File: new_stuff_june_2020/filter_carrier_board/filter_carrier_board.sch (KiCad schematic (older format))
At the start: 44 parts, among them J1 CV_inputs, J10 Conn_02x05_Odd_Even, J2 signal_inputs, J3 dry_out, J4 Conn_01x04, J5 Conn_01x04, J6 CV_out, J7 Conn_01x04, J8 Conn_01x08, J9 wet_out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

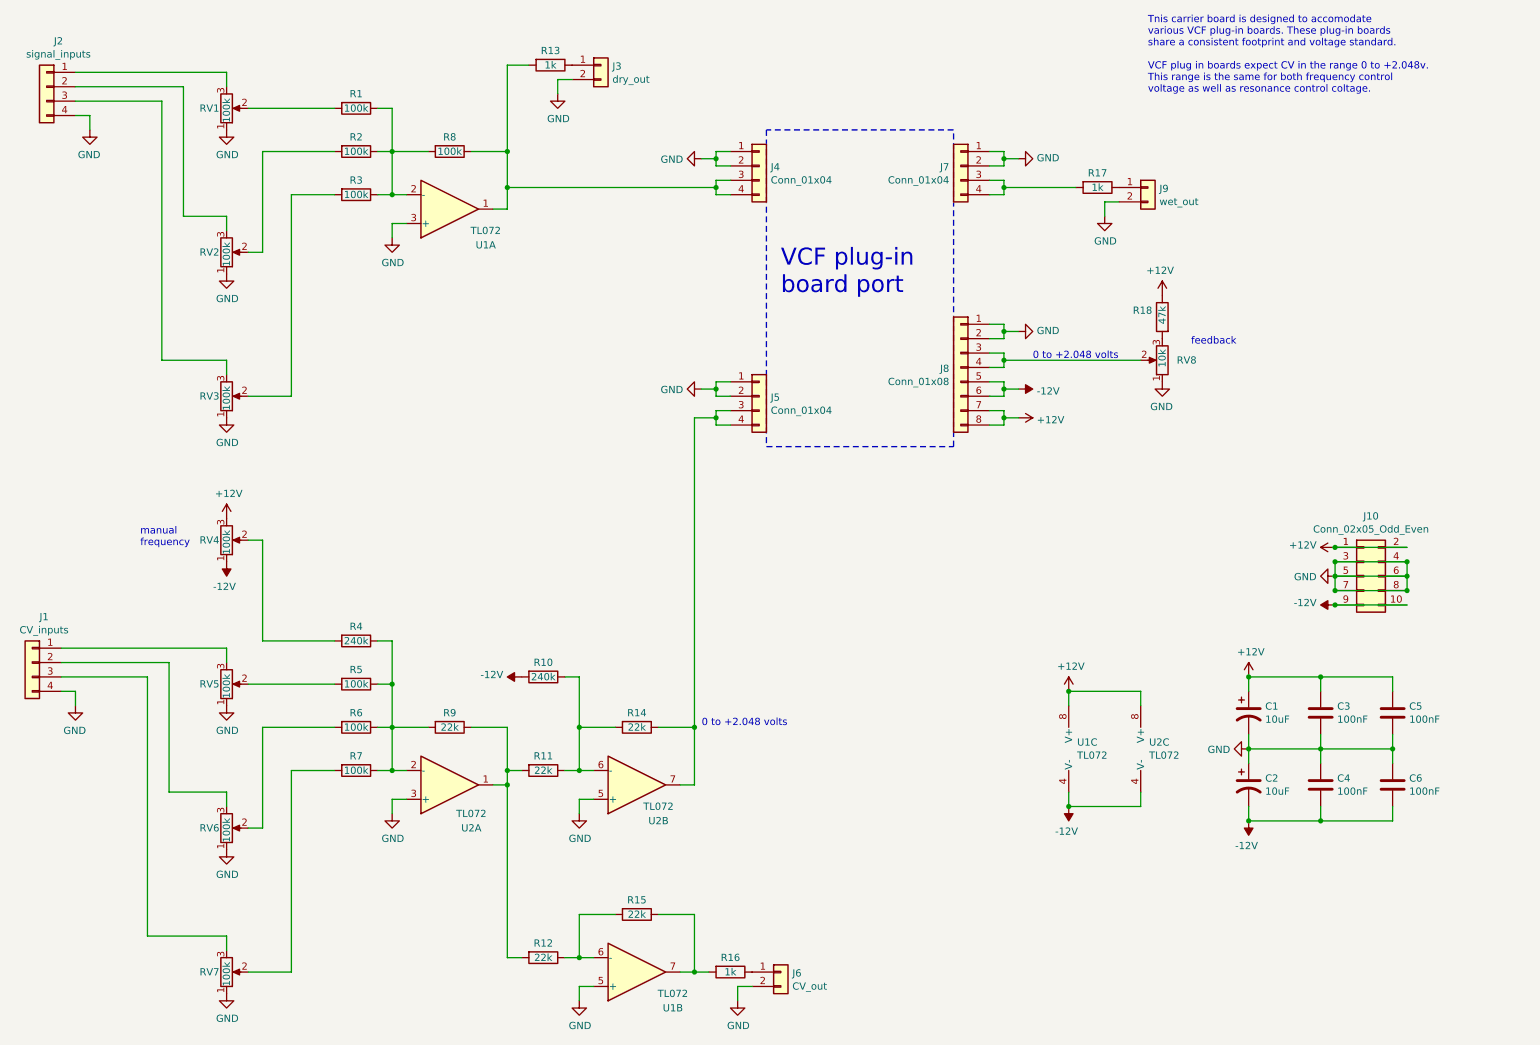
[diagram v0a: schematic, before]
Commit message: add +/- 5 volt ref to VCF carrier board
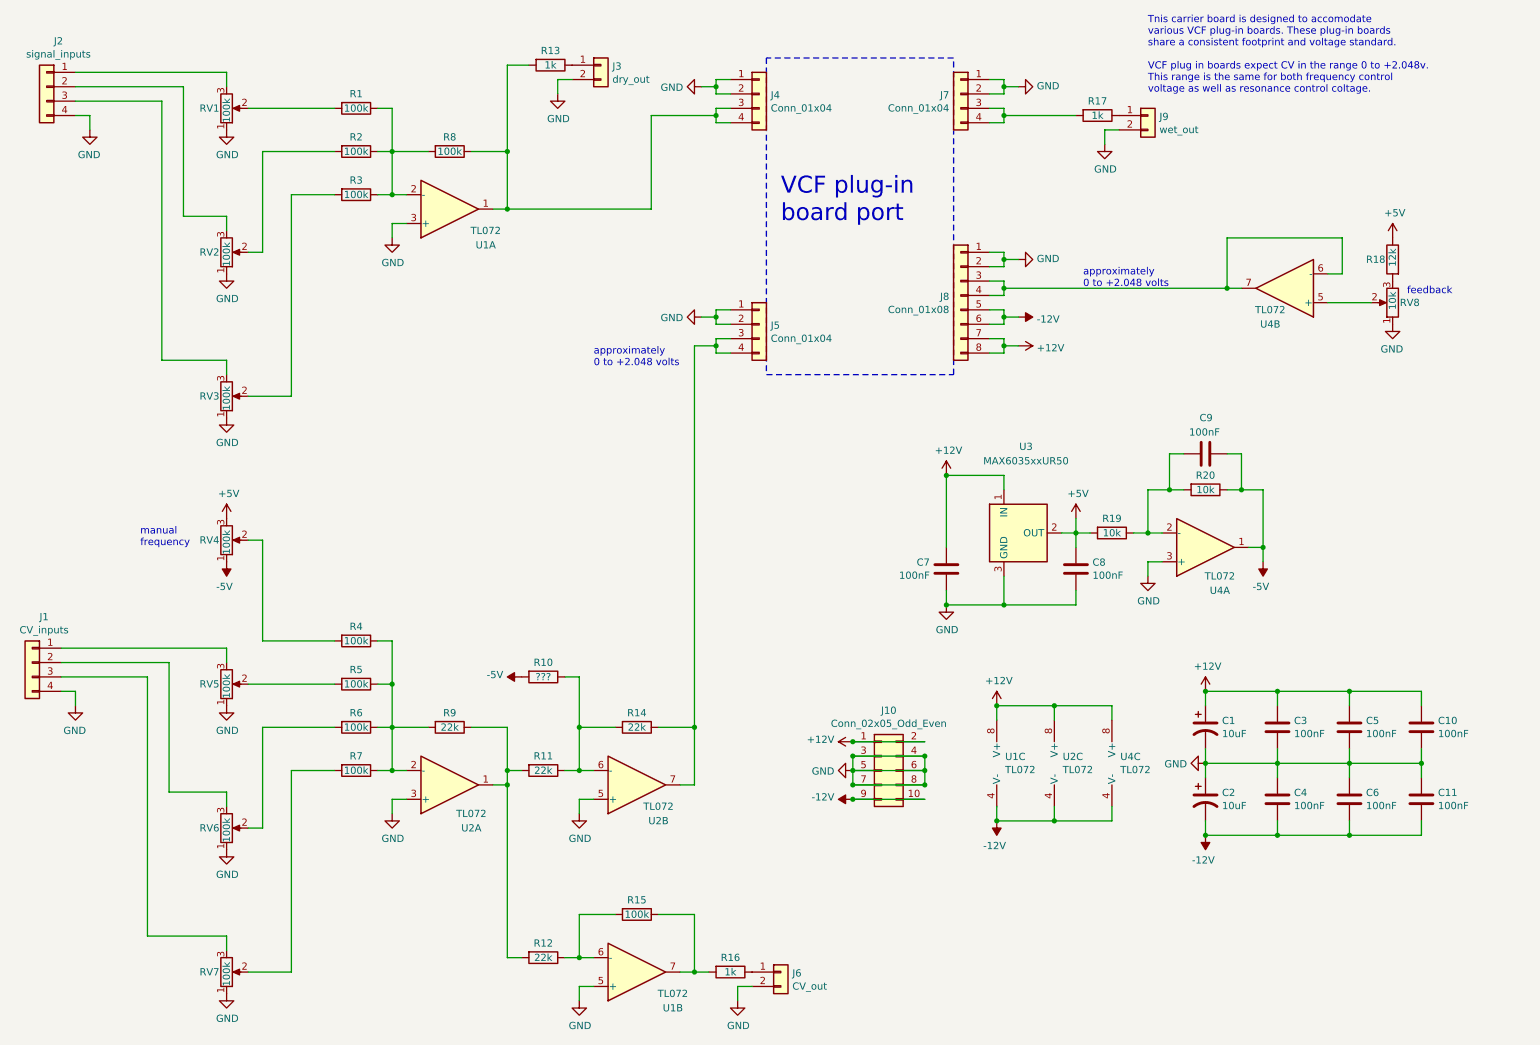
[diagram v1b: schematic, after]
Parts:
- added C10, C11, C7, C8, C9: 100nF, Capacitor_THT:C_Axial_L3.8mm_D2.6mm_P7.50mm_Horizontal, symbol Device:C
- added R19, R20: 10k, Resistor_THT:R_Axial_DIN0207_L6.3mm_D2.5mm_P10.16mm_Horizontal, symbol Device:R
- added U3: MAX6035xxUR50, Package_TO_SOT_SMD:SOT-23_Handsoldering, symbol Reference_Voltage:MAX6035xxUR50
- added U4: TL072, Package_DIP:DIP-8_W7.62mm, symbol Amplifier_Operational:TL072
- R10: value 240k -> ???
- R15: value 22k -> 100k
- R18: value 47k -> 12k
- R4: value 240k -> 100k
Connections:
- net +12V: now also C10.1, C7.1, U3.1 (IN), U4.8 (V+); no longer R18.1, RV4.3
- net -12V: now also C11.2, U4.4 (V-); no longer R10.2, RV4.1
- net GND: now also C10.2, C11.1, C7.2, C8.2, U3.3 (GND), U4.3 (+)
- net at J8.3 (Pin_3), J8.4 (Pin_4): now also U4.6 (-), U4.7; no longer RV8.2
- new net: C9.1, R19.1, R20.2, U4.2 (-)
- new net: RV8.2, U4.5 (+)
- new net +5V: C8.1, R18.1, R19.2, RV4.3, U3.2 (OUT)
- new net -5V: C9.2, R10.2, R20.1, RV4.1, U4.1
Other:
- note added: "approximately\n0 to +2.048 volts"
- note removed: "0 to +2.048 volts"
- moved on the sheet: C1, C2, C3, C4, C5, C6, J10, J4, J5, J7, J8, J9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
